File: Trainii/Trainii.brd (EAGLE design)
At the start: 160 x 100 mm, 29 parts, among them J1 apd, J2 left motor encoder, J3 right motor encoder, J4 line sensor 2, J5 line sensor 1, J6 ultrasonic, J7 left motor output, J8 right motor output, J9 lift motor output

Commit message: Changed a few parts, corrected small wiring connections, routed board
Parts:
- removed U$1: DRV8833, Tranii:DRV8833
- removed U$9: LM3671, Tranii:LM3671
- added MC1, MC2: DRV8833, Trainii:DRV8833
- added U1: TPS61222DCKR, Trainii:DCK6
- added U2: BSS138, Trainii:SOT-23-3L
- C2: value 0.1uF -> 10µF
- C3: value 10µF -> 0.1uF
- C5: value 4.7uF -> 10uF
- U$12: device Tranii:VLS3012HBX -> Trainii:VLS3012HBX
- U$2: value DRV8833 -> (none); device Tranii:DRV8833 -> RoboJackets-Aesthetics:ROBOBUZZ_0.4X
- U$6: device Tranii:ESP32 -> Trainii:ESP32
- U$8: value BSS138 -> (none); device Tranii:BSS138 -> RoboJackets-Aesthetics:ROBOJACKETS
- moved J1 191.6 mm to (62.2, 25.4), turned to 270 degrees
- moved J2 183.2 mm to (14.0, 34.3), turned to 90 degrees
- moved J3 176.6 mm to (14.0, 22.9), turned to 90 degrees
- moved J4 133.9 mm to (14.0, 57.1), turned to 90 degrees
- moved J6 132.5 mm to (34.3, 5.08)
- moved J5 128.4 mm to (14.0, 45.7), turned to 90 degrees
- moved U$2 81.6 mm to (10.2, 47.0), turned to 90 degrees
- moved R8 64.7 mm to (43.2, 17.8)
- moved J7 63.8 mm to (62.2, 50.8), turned to 90 degrees
- moved C1 63.8 mm to (47.0, 61.0), turned to 90 degrees
- moved R3 58.4 mm to (53.3, 66.0)
- moved R7 56.1 mm to (41.9, 12.7), turned to 90 degrees
- moved J9 50.8 mm to (62.2, 33.0), turned to 90 degrees
- moved R4 49.8 mm to (54.6, 53.3)
- moved C4 48.0 mm to (47.0, 36.8), turned to 270 degrees
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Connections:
- net OUT1 renamed LINE_OUT_1
- net OUT2 renamed LINE_OUT_2
- net TICKLEFT renamed TICK_LEFT
- net TICKRIGHT renamed TICK_RIGHT
- removed net LEFT0: J7.1, U$1.AOUT2
- removed net LEFT1: J7.2, U$1.AOUT1
- removed net LIFT0: J9.1, U$2.AOUT1
- removed net LIFT1: J9.2, U$2.AOUT2
- removed net N$2: C6.1, U$12.P$2, U$9.FB
- removed net RIGHT0: J8.1, U$1.BOUT1
- removed net RIGHT1: J8.2, U$1.BOUT2
- removed net VCC5: J6.1, R6.1
- new net +5V: C6.1, J6.1, R6.1, U1.2, U1.4
- new net LEFT_0: J7.1, MC1.AOUT1
- new net LEFT_1: J7.2, MC1.AOUT2
- new net LIFT_0: J9.1, MC2.AOUT1
- new net LIFT_1: J9.2, MC2.AOUT2
- new net RIGHT_0: J8.1, MC1.BOUT1
- new net RIGHT_1: J8.2, MC1.BOUT2
- net GND: now also C2.2, MC1.GND, MC1.GNDP, MC2.GND, MC2.GNDP, U1.3; no longer C3.2, U$1.GND, U$1.GNDP, U$2.GND, U$2.GNDP, U$9.GND
- net LEFT_A: now also MC1.AIN1; no longer U$1.AIN1
- net LEFT_B: now also MC1.AIN2; no longer U$1.AIN2
- net LIFT_A: now also MC2.AIN1; no longer U$2.AIN1
- net LIFT_B: now also MC2.AIN2; no longer U$2.AIN2
- net N$1: now also U1.5; no longer U$9.SW
- net N$10: now also MC1.AISEN; no longer U$1.AISEN
- net N$3: now also C3.2, MC2.VCP; no longer C2.2, U$2.VCP
- net N$4: now also MC2.BISEN; no longer U$2.BISEN
- net N$5: now also C4.1, MC2.VINT; no longer C3.1, U$2.VINT
- net N$6: now also MC2.AISEN; no longer U$2.AISEN
- net N$7: now also MC1.VCP; no longer U$1.VCP
- net N$8: now also C2.1, MC1.VINT; no longer C4.1, U$1.VINT
- net N$9: now also MC1.BISEN; no longer U$1.BISEN
- net RIGHT_A: now also MC1.BIN1; no longer U$1.BIN1
- net RIGHT_B: now also MC1.BIN2; no longer U$1.BIN2
- net TRIG: now also U2.3; no longer U$8.D
- net TRIG3.3: now also U2.2; no longer U$8.S
- net VCC: now also C3.1, MC1.NSLEEP, MC1.VM, MC2.NSLEEP, MC2.VM, U$12.P$2, U1.1, U1.6, U2.1; no longer C2.1, U$1.NSLEEP, U$1.VM, U$2.NSLEEP, U$2.VM, U$8.G, U$9.EN, U$9.VIN
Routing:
- net VCC: track 0.00 -> 169.2 mm, vias 0 -> 4
- net GND: track 0.00 -> 58.8 mm, vias 0 -> 6
- net 3V: track 0.00 -> 49.3 mm
- net TRIG3.3: track 0.00 -> 47.5 mm
- net RIGHT_B: track 0.00 -> 43.0 mm
- net LEFT_A: track 0.00 -> 32.8 mm, vias 0 -> 1
- net RIGHT_A: track 0.00 -> 31.2 mm
- net SCL: track 0.00 -> 28.7 mm
- net ECHO3.3: track 0.00 -> 27.2 mm
- net SDA: track 0.00 -> 22.5 mm
- net +5V: track 0.00 -> 19.6 mm
- net TICK_RIGHT: track 0.00 -> 17.4 mm
- net LINE_OUT_1: track 0.00 -> 16.5 mm
- net LEFT_B: track 0.00 -> 15.6 mm
- net LIFT_B: track 0.00 -> 15.3 mm
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- added copper zone on layer 16, net GND
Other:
- board size 160 x 100 mm -> 71.1 x 71.1 mm

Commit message: Ran design rule checks
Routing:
- net 3V: track 49.3 -> 55.1 mm
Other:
- outline, holes or cut-outs redrawn
- board text added: "May 2018"
- board text added: "New Member Training Robot"
- board text added: "Trainii"
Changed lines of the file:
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@@
 <board>
 <plain>
-<wire x1="0" y1="0" x2="71.12" y2="0" width="0" layer="20"/>
-<wire x1="71.12" y1="0" x2="71.12" y2="71.12" width="0" layer="20"/>
-<wire x1="71.12" y1="71.12" x2="0" y2="71.12" width="0" layer="20"/>
-<wire x1="0" y1="71.12" x2="0" y2="0" width="0" layer="20"/>
+<wire x1="68.58" y1="71.12" x2="2.54" y2="71.12" width="0" layer="20"/>
+<wire x1="2.54" y1="71.12" x2="0" y2="68.58" width="0" layer="20" curve="90"/>
+<wire x1="0" y1="68.58" x2="0" y2="2.54" width="0" layer="20"/>
+<wire x1="0" y1="2.54" x2="2.54" y2="0" width="0" layer="20" curve="90"/>
+<wire x1="2.54" y1="0" x2="68.58" y2="0" width="0" layer="20"/>
+<wire x1="68.58" y1="0" x2="71.12" y2="2.54" width="0" layer="20" curve="90"/>
+<wire x1="71.12" y1="2.54" x2="71.12" y2="68.58" width="0" layer="20"/>
+<wire x1="71.12" y1="68.58" x2="68.58" y2="71.12" width="0" layer="20" curve="90"/>
 <hole x="3.81" y="67.31" drill="3.5052"/>
 <hole x="67.31" y="67.31" drill="3.5052"/>
 <hole x="3.81" y="3.81" drill="3.5052"/>
 <hole x="67.31" y="3.81" drill="3.5052"/>
+<text x="27.94" y="27.94" size="1.778" layer="21" font="vector" ratio="20" rot="R90">Trainii</text>
+<text x="30.48" y="27.94" size="1.778" layer="21" font="vector" ratio="20" rot="R90">New Member Training Robot</text>
+<text x="33.02" y="27.94" size="1.778" layer="21" font="vector" ratio="20" rot="R90">May 2018</text>
+<wire x1="30.48" y1="71.12" x2="30.48" y2="69.85" width="0.3048" layer="21"/>
+<wire x1="30.48" y1="69.85" x2="34.29" y2="69.85" width="0.3048" layer="21"/>
+<wire x1="34.29" y1="69.85" x2="34.29" y2="71.12" width="0.3048" layer="21"/>
 </plain>
 <attributes>
@@
 </class>
 </classes>
-<designrules name="default">
+<designrules name="SeeedStudio">
 <description language="de">&lt;b&gt;EAGLE Design Rules&lt;/b&gt;
 &lt;p&gt;
@@
 necessary adjustments and save your customized
 design rules under a new name.</description>
+<description language="zh">&lt;b&gt;Seeed Studio EAGLE Design Rules&lt;/b&gt;
+</description>
 <param name="layerSetup" value="(1*16)"/>
-<param name="mtCopper" value="0.035mm 0.035mm 0.035mm 0.035mm 0.035mm 0.035mm 0.035mm 0.035mm 0.035mm 0.035mm 0.035mm 0.035mm 0.035mm 0.035mm 0.035mm 0.035mm"/>
-<param name="mtIsolate" value="1.5mm 0.15mm 0.2mm 0.15mm 0.2mm 0.15mm 0.2mm 0.15mm 0.2mm 0.15mm 0.2mm 0.15mm 0.2mm 0.15mm 0.2mm"/>
+<param name="mtCopper" value="0.035mm 0.0175mm 0.035mm 0.035mm 0.035mm 0.035mm 0.035mm 0.035mm 0.035mm 0.035mm 0.035mm 0.035mm 0.035mm 0.035mm 0.0175mm 0.035mm"/>
+<param name="mtIsolate" value="1.5mm 1.1mm 0.2mm 0.15mm 0.2mm 0.15mm 0.2mm 0.15mm 0.2mm 0.15mm 0.2mm 0.15mm 0.2mm 0.15mm 0.2mm"/>
 <param name="mdWireWire" value="6mil"/>
 <param name="mdWirePad" value="6mil"/>
@@
 <param name="mdPadVia" value="6mil"/>
 <param name="mdViaVia" value="6mil"/>
-<param name="mdSmdPad" value="6mil"/>
-<param name="mdSmdVia" value="6mil"/>
-<param name="mdSmdSmd" value="6mil"/>
-<param name="mdViaViaSameLayer" value="6mil"/>
+<param name="mdSmdPad" value="0mil"/>
+<param name="mdSmdVia" value="0mil"/>
+<param name="mdSmdSmd" value="0mil"/>
+<param name="mdViaViaSameLayer" value="8mil"/>
 <param name="mnLayersViaInSmd" value="2"/>
-<param name="mdCopperDimension" value="40mil"/>
-<param name="mdDrill" value="6mil"/>
+<param name="mdCopperDimension" value="10mil"/>
+<param name="mdDrill" value="10mil"/>
 <param name="mdSmdStop" value="0mil"/>
 <param name="msWidth" value="6mil"/>
-<param name="msDrill" value="0.35mm"/>
-<param name="msMicroVia" value="9.99mm"/>
+<param name="msDrill" value="12mil"/>
+<param name="msMicroVia" value="12mil"/>
 <param name="msBlindViaRatio" value="0.5"/>
 <param name="rvPadTop" value="0.25"/>
@@
 <param name="rlMinPadBottom" value="10mil"/>
 <param name="rlMaxPadBottom" value="20mil"/>
-<param name="rlMinViaOuter" value="8mil"/>
+<param name="rlMinViaOuter" value="6mil"/>
 <param name="rlMaxViaOuter" value="20mil"/>
-<param name="rlMinViaInner" value="8mil"/>
+<param name="rlMinViaInner" value="6mil"/>
 <param name="rlMaxViaInner" value="20mil"/>
 <param name="rlMinMicroViaOuter" value="4mil"/>
@@
 <param name="psTop" value="-1"/>
 <param name="psBottom" value="-1"/>
-<param name="psFirst" value="-1"/>
+<param name="psFirst" value="0"/>
 <param name="psElongationLong" value="100"/>
 <param name="psElongationOffset" value="100"/>
 <param name="mvStopFrame" value="1"/>
 <param name="mvCreamFrame" value="0"/>
-<param name="mlMinStopFrame" value="4mil"/>
-<param name="mlMaxStopFrame" value="4mil"/>
+<param name="mlMinStopFrame" value="2mil"/>
+<param name="mlMaxStopFrame" value="2mil"/>
 <param name="mlMinCreamFrame" value="0mil"/>
 <param name="mlMaxCreamFrame" value="0mil"/>
-<param name="mlViaStopLimit" value="0mil"/>
+<param name="mlViaStopLimit" value="100mil"/>
 <param name="srRoundness" value="0"/>
 <param name="srMinRoundness" value="0mil"/>
@@
 <param name="checkAngle" value="0"/>
 <param name="checkFont" value="1"/>
-<param name="checkRestrict" value="1"/>
+<param name="checkRestrict" value="0"/>
 <param name="checkStop" value="0"/>
 <param name="checkValues" value="0"/>
@@
 <contactref element="R8" pad="2"/>
 <polygon width="0.254" layer="16" isolate="0.4064">
-<vertex x="0" y="71.12"/>
-<vertex x="71.12" y="71.12"/>
-<vertex x="71.12" y="0"/>
-<vertex x="0" y="0"/>
+<vertex x="0" y="2.54"/>
+<vertex x="0" y="68.58" curve="-90"/>
+<vertex x="2.54" y="71.12"/>
+<vertex x="68.58" y="71.12" curve="-90"/>
+<vertex x="71.12" y="68.58"/>
+<vertex x="71.12" y="2.54" curve="-90"/>
+<vertex x="68.58" y="0"/>
+<vertex x="2.54" y="0" curve="-90"/>
 </polygon>
 <contactref element="U1" pad="3"/>
@@
 <contactref element="J2" pad="1"/>
 <contactref element="J3" pad="1"/>
-<wire x1="12.7" y1="35.56" x2="12.7" y2="46.99" width="0.4064" layer="16"/>
-<wire x1="12.6746" y1="28.476575" x2="12.7" y2="28.501975" width="0.4064" layer="16"/>
-<wire x1="12.7" y1="28.501975" x2="12.7" y2="33.02" width="0.4064" layer="16"/>
-<wire x1="12.6746" y1="24.1554" x2="12.6746" y2="28.476575" width="0.4064" layer="16"/>
-<wire x1="13.97" y1="22.86" x2="12.6746" y2="24.1554" width="0.4064" layer="16"/>
-<wire x1="12.7" y1="33.02" x2="13.97" y2="34.29" width="0.4064" layer="16"/>
-<wire x1="13.97" y1="34.29" x2="12.7" y2="35.56" width="0.4064" layer="16"/>
-<wire x1="12.7" y1="46.99" x2="13.97" y2="48.26" width="0.4064" layer="16"/>
 <wire x1="13.97" y1="48.26" x2="13.97" y2="48.968025" width="0.4064" layer="16"/>
-<wire x1="12.6746" y1="57.686575" x2="12.7" y2="57.711975" width="0.4064" layer="16"/>
-<wire x1="12.7" y1="57.711975" x2="12.7" y2="58.42" width="0.4064" layer="16"/>
-<wire x1="13.97" y1="48.968025" x2="12.6746" y2="50.263425" width="0.4064" layer="16"/>
-<wire x1="12.6746" y1="50.263425" x2="12.6746" y2="57.686575" width="0.4064" layer="16"/>
-<wire x1="12.7" y1="58.42" x2="13.97" y2="59.69" width="0.4064" layer="16"/>
 <wire x1="13.97" y1="59.69" x2="19.685" y2="59.69" width="0.4064" layer="16"/>
 <wire x1="19.685" y1="59.69" x2="22.225" y2="62.23" width="0.4064" layer="16"/>
+<wire x1="13.97" y1="22.86" x2="12.7" y2="22.86" width="0.4064" layer="16"/>
+<wire x1="12.7" y1="22.86" x2="11.43" y2="24.13" width="0.4064" layer="16"/>
+<wire x1="11.43" y1="24.13" x2="11.43" y2="33.02" width="0.4064" layer="16"/>
+<wire x1="11.43" y1="33.02" x2="12.7" y2="34.29" width="0.4064" layer="16"/>
+<wire x1="12.7" y1="34.29" x2="13.97" y2="34.29" width="0.4064" layer="16"/>
+<wire x1="12.7" y1="34.29" x2="11.43" y2="35.56" width="0.4064" layer="16"/>
+<wire x1="12.7" y1="48.26" x2="11.43" y2="46.99" width="0.4064" layer="16"/>
+<wire x1="11.43" y1="35.56" x2="11.43" y2="46.99" width="0.4064" layer="16"/>
+<wire x1="13.97" y1="48.26" x2="12.7" y2="48.26" width="0.4064" layer="16"/>
+<wire x1="12.7" y1="48.26" x2="11.43" y2="49.53" width="0.4064" layer="16"/>
+<wire x1="11.43" y1="49.53" x2="11.43" y2="58.42" width="0.4064" layer="16"/>
+<wire x1="11.43" y1="58.42" x2="12.7" y2="59.69" width="0.4064" layer="16"/>
+<wire x1="12.7" y1="59.69" x2="13.97" y2="59.69" width="0.4064" layer="16"/>
 </signal>
 <signal name="TICK_RIGHT">

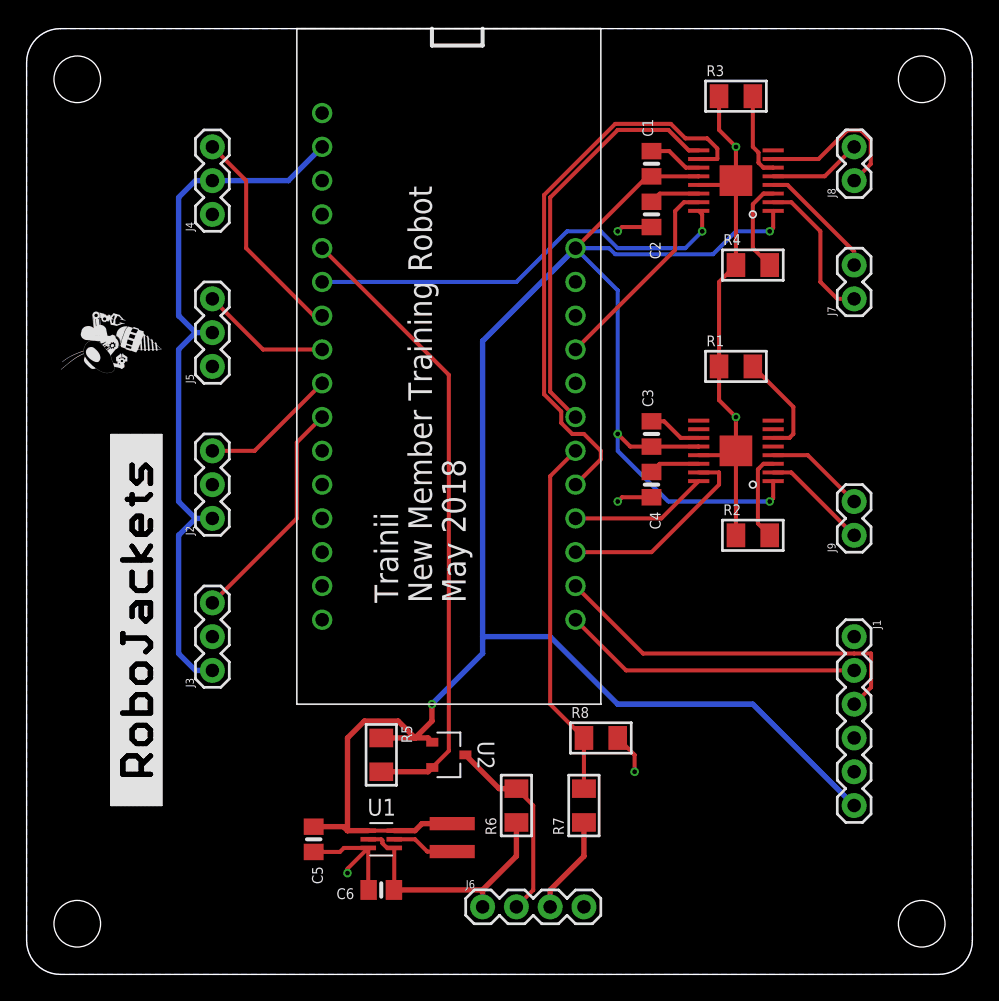
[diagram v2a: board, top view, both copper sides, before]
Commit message: Squeezes board to 2in width.
Re-layout to try to fit board into last draft of the mechanical CAD.
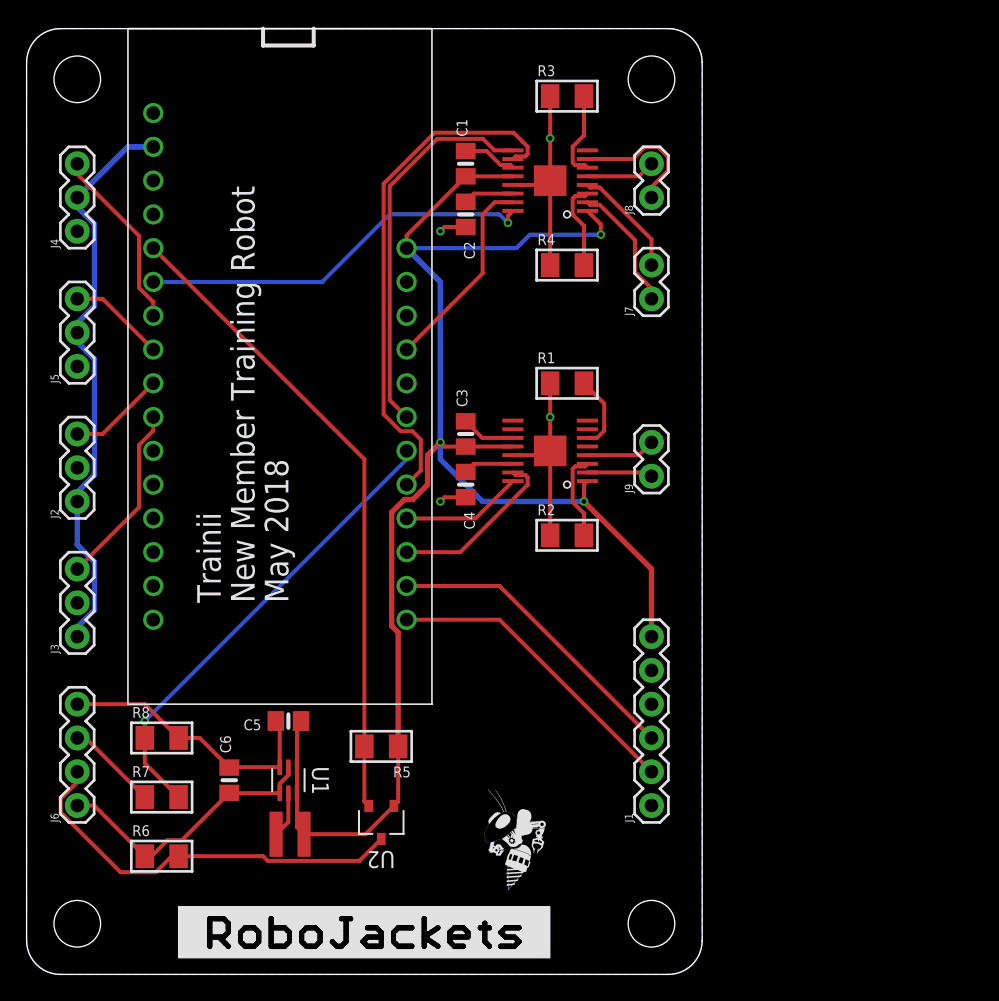
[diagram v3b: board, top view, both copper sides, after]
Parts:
- moved U$2 48.3 mm to (36.2, 6.35), turned to 0 degrees
- moved R8 33.0 mm to (10.2, 17.8)
- moved R7 31.8 mm to (10.2, 13.3), turned to 0 degrees
- moved J6 31.4 mm to (3.81, 12.7), turned to 90 degrees
- moved R6 26.9 mm to (10.2, 8.89), turned to 0 degrees
- moved J1 19.8 mm to (47.0, 12.7), turned to 90 degrees
- moved J9 15.9 mm to (47.0, 37.5)
- moved J8 15.3 mm to (47.0, 58.4)
- moved J7 15.2 mm to (47.0, 50.8)
- moved C6 14.1 mm to (15.2, 14.6), turned to 90 degrees
- moved MC1 14.0 mm to (39.4, 59.7)
- moved MC2 14.0 mm to (39.4, 39.4)
- moved C1 14.0 mm to (33.0, 61.0)
- moved C2 14.0 mm to (33.0, 57.1)
- moved C3 14.0 mm to (33.0, 40.6)
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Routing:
- net VCC: track 169.2 -> 122.6 mm, vias 4 -> 3
- net TRIG: track 14.8 -> 30.9 mm
- net 3V: track 55.1 -> 43.5 mm
- net ECHO3.3: track 27.2 -> 35.2 mm, vias 0 -> 1
- net SCL: track 28.7 -> 23.1 mm
- net GND: track 58.8 -> 55.1 mm, vias 6 -> 4
- net RIGHT_B: track 43.0 -> 39.4 mm
- net TICK_RIGHT: track 17.4 -> 13.8 mm
- net LIFT_0: track 8.05 -> 4.94 mm
- net TICK_LEFT: track 10.4 -> 7.29 mm
- net LEFT_A: track 32.8 -> 30.1 mm
- net LINE_OUT_1: track 16.5 -> 13.8 mm
- net LINE_OUT_2: track 9.83 -> 7.29 mm
- net LIFT_B: track 15.3 -> 13.0 mm
- net LIFT_1: track 7.53 -> 5.22 mm
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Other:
- board size 71.1 x 71.1 mm -> 50.8 x 71.1 mm
